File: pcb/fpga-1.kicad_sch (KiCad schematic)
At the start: 7 parts, among them U7 XC7A100T-FGG484

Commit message: restructured power, power plane layout
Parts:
- renumbered C17 to C16, C18 to C17, C19 to C18, C20 to C19, C21 to C20, C22 to C21, U7 to U4
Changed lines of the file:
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@@
 		(dnp no)
 		(fields_autoplaced yes)
-		(property "Reference" "U7"
+		(property "Reference" "U4"
 			(at 121.92 20.32 0)
 			(effects
@@
 			(project "RPi-HwAB-1"
 				(path "/e63e39d7-6ac0-4ffd-8aa3-1841a4541b55/59d21473-a004-4514-8090-fd93db818925/350bfe7d-9948-4ca7-a542-a75eb385def4"
-					(reference "U7")
+					(reference "U4")
 					(unit 2)
 				)
@@
 		(dnp no)
 		(fields_autoplaced yes)
-		(property "Reference" "#PWR023"
+		(property "Reference" "#PWR020"
 			(at 243.84 110.49 0)
 			(effects
@@
 			(project ""
 				(path "/e63e39d7-6ac0-4ffd-8aa3-1841a4541b55/59d21473-a004-4514-8090-fd93db818925/350bfe7d-9948-4ca7-a542-a75eb385def4"
-					(reference "#PWR023")
+					(reference "#PWR020")
 					(unit 1)
 				)
@@
 		(on_board yes)
 		(dnp no)
-		(property "Reference" "C22"
+		(property "Reference" "C21"
 			(at 232.41 143.51 0)
 			(effects
@@
 			(project "RPi-HwAB-1"
 				(path "/e63e39d7-6ac0-4ffd-8aa3-1841a4541b55/59d21473-a004-4514-8090-fd93db818925/350bfe7d-9948-4ca7-a542-a75eb385def4"
-					(reference "C22")
+					(reference "C21")
 					(unit 1)
 				)
@@
 		(on_board yes)
 		(dnp no)
-		(property "Reference" "C21"
+		(property "Reference" "C20"
 			(at 224.79 143.51 0)
 			(effects
@@
 			(project "RPi-HwAB-1"
 				(path "/e63e39d7-6ac0-4ffd-8aa3-1841a4541b55/59d21473-a004-4514-8090-fd93db818925/350bfe7d-9948-4ca7-a542-a75eb385def4"
-					(reference "C21")
+					(reference "C20")
 					(unit 1)
 				)
@@
 		(on_board yes)
 		(dnp no)
-		(property "Reference" "C18"
+		(property "Reference" "C17"
 			(at 201.93 143.51 0)
 			(effects
@@
 			(project "RPi-HwAB-1"
 				(path "/e63e39d7-6ac0-4ffd-8aa3-1841a4541b55/59d21473-a004-4514-8090-fd93db818925/350bfe7d-9948-4ca7-a542-a75eb385def4"
-					(reference "C18")
+					(reference "C17")
 					(unit 1)
 				)
@@
 		(dnp no)
 		(fields_autoplaced yes)
-		(property "Reference" "U7"
+		(property "Reference" "U4"
 			(at 223.52 20.32 0)
 			(effects
@@
 			(project "RPi-HwAB-1"
 				(path "/e63e39d7-6ac0-4ffd-8aa3-1841a4541b55/59d21473-a004-4514-8090-fd93db818925/350bfe7d-9948-4ca7-a542-a75eb385def4"
-					(reference "U7")
+					(reference "U4")
 					(unit 8)
 				)
@@
 		(on_board yes)
 		(dnp no)
-		(property "Reference" "C17"
+		(property "Reference" "C16"
 			(at 257.81 95.25 0)
 			(effects
@@
 			(project "RPi-HwAB-1"
 				(path "/e63e39d7-6ac0-4ffd-8aa3-1841a4541b55/59d21473-a004-4514-8090-fd93db818925/350bfe7d-9948-4ca7-a542-a75eb385def4"
-					(reference "C17")
+					(reference "C16")
 					(unit 1)
 				)
@@
 		(on_board yes)
 		(dnp no)
-		(property "Reference" "C19"
+		(property "Reference" "C18"
 			(at 209.55 143.51 0)
 			(effects
@@
 			(project "RPi-HwAB-1"
 				(path "/e63e39d7-6ac0-4ffd-8aa3-1841a4541b55/59d21473-a004-4514-8090-fd93db818925/350bfe7d-9948-4ca7-a542-a75eb385def4"
-					(reference "C19")
+					(reference "C18")
 					(unit 1)
 				)
@@
 		(on_board yes)
 		(dnp no)
-		(property "Reference" "U7"
+		(property "Reference" "U4"
 			(at 40.64 22.86 0)
 			(effects
@@
 			(project "RPi-HwAB-1"
 				(path "/e63e39d7-6ac0-4ffd-8aa3-1841a4541b55/59d21473-a004-4514-8090-fd93db818925/350bfe7d-9948-4ca7-a542-a75eb385def4"
-					(reference "U7")
+					(reference "U4")
 					(unit 1)
 				)
@@
 		(dnp no)
 		(fields_autoplaced yes)
-		(property "Reference" "#PWR025"
+		(property "Reference" "#PWR022"
 			(at 231.14 161.29 0)
 			(effects
@@
 			(project "RPi-HwAB-1"
 				(path "/e63e39d7-6ac0-4ffd-8aa3-1841a4541b55/59d21473-a004-4514-8090-fd93db818925/350bfe7d-9948-4ca7-a542-a75eb385def4"
-					(reference "#PWR025")
+					(reference "#PWR022")
 					(unit 1)
 				)
@@
 		(on_board yes)
 		(dnp no)
-		(property "Reference" "C20"
+		(property "Reference" "C19"
 			(at 217.17 143.51 0)
 			(effects
@@
 			(project "RPi-HwAB-1"
 				(path "/e63e39d7-6ac0-4ffd-8aa3-1841a4541b55/59d21473-a004-4514-8090-fd93db818925/350bfe7d-9948-4ca7-a542-a75eb385def4"
-					(reference "C20")
+					(reference "C19")
 					(unit 1)
 				)
@@
 		(dnp no)
 		(fields_autoplaced yes)
-		(property "Reference" "#PWR024"
+		(property "Reference" "#PWR021"
 			(at 256.54 110.49 0)
 			(effects
@@
 			(project "RPi-HwAB-1"
 				(path "/e63e39d7-6ac0-4ffd-8aa3-1841a4541b55/59d21473-a004-4514-8090-fd93db818925/350bfe7d-9948-4ca7-a542-a75eb385def4"
-					(reference "#PWR024")
+					(reference "#PWR021")
 					(unit 1)
 				)

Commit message: complete! added and prettied up silkscreen
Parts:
- added D1: LED Green, LED_SMD:LED_0603_1608Metric, symbol library:LED
- added D3: LED Blue, LED_SMD:LED_0603_1608Metric, symbol library:LED
- added R38: 1k, Resistor_SMD:R_0402_1005Metric, symbol library:R_US
- added R39, R42: 4.7K, Resistor_SMD:R_0402_1005Metric, symbol library:R_US
- added R41: 330, Resistor_SMD:R_0402_1005Metric, symbol library:R_US
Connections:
- net 3V3_FD: now also U4.U11 (M0_0), U4.U8 (CFGBVS_0), R38.2, R39.2, R42.2
- net DONE: now also D1.1 (K)
- net GND: now also U4.L10 (VP_0), U4.L9 (VREFN_0), U4.M10 (VREFP_0), U4.M9 (VN_0), U4.U10 (M1_0), U4.U9 (M2_0), D3.1 (K)
- net PROG_B: now also R39.1
- net LED1: now reaches U4.Y21 (IO_L9P_T1_DQS_14)
- net LED1: now also R41.1
- net INIT_B: now reaches U4.U12 (INIT_B_0)
- net INIT_B: now also R42.1
- new net: D3.2 (A), R41.2
- new net: D1.2 (A), R38.1
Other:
- moved on the sheet: C16, U4H

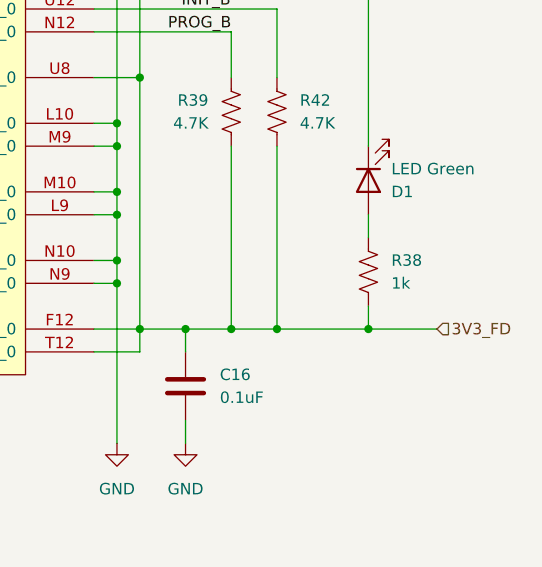
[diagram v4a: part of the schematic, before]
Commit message: added jlc fab
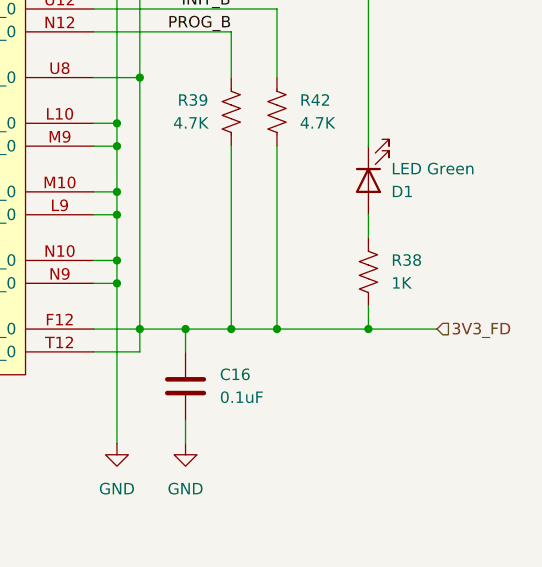
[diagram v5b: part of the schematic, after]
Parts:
- D1: Manufacturer Product Number LTST-S270KGKT -> LTST-C190GKT; Part Description (none) -> LED GREEN CLEAR CHIP SMD
- D3: Manufacturer Product Number LTST-S270TBKT -> LTST-C190TBKT; Part Description (none) -> LED BLUE CLEAR CHIP SMD
- R38: value 1k -> 1K; Part Description (none) -> RES 1K OHM 5% 1/16W 0402
- R41: Part Description (none) -> RES 330 OHM 1% 1/16W 0402
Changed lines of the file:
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@@
+			)
+		)
+		(property "Part Description" "RES 330 OHM 1% 1/16W 0402"
+			(at 190.5 77.47 0)
+			(hide yes)
+			(show_name no)
+			(do_not_autoplace no)
+			(effects
+				(font
+					(size 1.27 1.27)
+				)
 			)
 		)
@@
 			)
 		)
-		(property "Value" "1k"
+		(property "Value" "1K"
 			(at 266.7 86.36 0)
 			(show_name no)
@@
 		)
 		(property "Manufacturer Product Number" "RC0402JR-071KL"
+			(at 264.16 85.09 0)
+			(hide yes)
+			(show_name no)
+			(do_not_autoplace no)
+			(effects
+				(font
+					(size 1.27 1.27)
+				)
+			)
+		)
+		(property "Part Description" "RES 1K OHM 5% 1/16W 0402"
 			(at 264.16 85.09 0)
 			(hide yes)
@@
 			)
 		)
-		(property "Manufacturer Product Number" "LTST-S270TBKT"
+		(property "Manufacturer Product Number" "LTST-C190TBKT"
+			(at 190.5 87.63 90)
+			(hide yes)
+			(show_name no)
+			(do_not_autoplace no)
+			(effects
+				(font
+					(size 1.27 1.27)
+				)
+			)
+		)
+		(property "Part Description" "LED BLUE CLEAR CHIP SMD"
 			(at 190.5 87.63 90)
 			(hide yes)
@@
 			)
 		)
-		(property "Datasheet" "http://optoelectronics.liteon.com/upload/download/DS22-2000-226/LTST-S270KGKT.pdf"
+		(property "Datasheet" ""
 			(at 264.16 74.93 0)
 			(hide yes)
@@
 			)
 		)
-		(property "Manufacturer Product Number" "LTST-S270KGKT"
+		(property "Manufacturer Product Number" "LTST-C190GKT"
 			(at 264.16 74.93 0)
 			(hide yes)
 			(show_name no)
+			(do_not_autoplace no)
+			(effects
+				(font
+					(size 1.27 1.27)
+				)
+			)
+		)
+		(property "Part Description" "LED GREEN CLEAR CHIP SMD"
+			(at 264.16 74.93 90)
+			(hide yes)
+			(show_name no)
